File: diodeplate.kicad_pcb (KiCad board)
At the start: 2 copper layers, 86 parts, among them U1 TS-1185EC-C-D-B, U10 CP2102-GMR, U11 U262-16XN-4BVC11, U14 UMH3N, U2 TS-1185EC-C-D-B, U3 TS-1185EC-C-D-B, U8 ESP32-WROOM-32E(4MB), U9 SN74AHCT32QPWRQ1

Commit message: add first pcb design
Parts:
- removed C13: 10uF, Capacitor_SMD:C_0603_1608Metric_Pad1.08x0.95mm_HandSolder
- removed REF1: BL1117-33CX, footprint:SOT-223-4_L6.5-W3.5-P2.30-LS7.0-BR
- removed U10: CP2102-GMR, footprint:QFN-28_L5.0-W5.0-P0.50-BL-EP
- removed U11: U262-16XN-4BVC11, footprint:USB-3.1-SMD_U262-161N-4BVC11
- removed U14: UMH3N, footprint:SC-70-6_L2.2-W1.3-P0.65-LS2.1-BR
- removed U8: ESP32-WROOM-32E(4MB), footprint:WIFI-SMD_ESP32-WROOM-32E
- removed U9: SN74AHCT32QPWRQ1, footprint:TSSOP-14_L5.0-W4.4-P0.65-LS6.5-BL
- added SW1: TS-1185EC-C-D-B, footprint:SW-SMD_4P-L3.7-W3.0-P1.50-LS4.7, F.Cu at (170.8, 151.2)
- added SW2: TS-1185EC-C-D-B, footprint:SW-SMD_4P-L3.7-W3.0-P1.50-LS4.7, F.Cu at (171.0, 156.2)
- added SW3: TS-1185EC-C-D-B, footprint:SW-SMD_4P-L3.7-W3.0-P1.50-LS4.7, F.Cu at (170.8, 144.8)
- added U4: BL1117-33CX, footprint:SOT-223-4_L6.5-W3.5-P2.30-LS7.0-BR, F.Cu at (225.0, 186.5)
- added U5: UMH3N, footprint:SC-70-6_L2.2-W1.3-P0.65-LS2.1-BR, F.Cu at (223.7, 143.1)
- added U6: SN74AHCT32QPWRQ1, footprint:TSSOP-14_L5.0-W4.4-P0.65-LS6.5-BL, F.Cu at (188.5, 99.8)
- U1: value TS-1185EC-C-D-B -> ESP32-WROOM-32E; footprint footprint:SW-SMD_4P-L3.7-W3.0-P1.50-LS4.7 -> footprint:WIFI-SMD_ESP32-WROOM-32E
- U2: value TS-1185EC-C-D-B -> CP2102-GMR; footprint footprint:SW-SMD_4P-L3.7-W3.0-P1.50-LS4.7 -> footprint:QFN-28_L5.0-W5.0-P0.50-BL-EP
- U3: value TS-1185EC-C-D-B -> U262-161N-4BVC11; footprint footprint:SW-SMD_4P-L3.7-W3.0-P1.50-LS4.7 -> footprint:USB-3.1-SMD_U262-161N-4BVC11
- moved LED24 179.9 mm to (289.5, 126.9)
- moved LED20 173.1 mm to (280.3, 181.3)
- moved LED18 169.3 mm to (260.5, 202.8)
- moved LED25 163.6 mm to (285.4, 114.2)
- moved LED16 163.0 mm to (237.3, 214.1)
- moved LED19 157.8 mm to (272.3, 192.2)
- moved LED23 152.1 mm to (291.1, 142.6)
- moved LED21 149.9 mm to (285.5, 170.8)
- moved C16 149.8 mm to (232.2, 196.9), turned to 90 degrees
- moved LED17 146.0 mm to (248.9, 209.7)
- moved C30 145.1 mm to (287.1, 142.2), turned to -90 degrees
- moved C33 143.6 mm to (274.9, 101.4), turned to -90 degrees
- moved LED22 142.6 mm to (289.8, 156.6)
- moved LED29 142.0 mm to (252.6, 77.4)
- moved C29 139.1 mm to (285.9, 156.2), turned to -90 degrees
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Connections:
- C1 pad 1: GND -> +3V3
- C1 pad 2: +3V3 -> GND
- U1 pad 2: Net-(R4-Pad1) -> +3V3
- U2 pad 1: GND -> unconnected-(U2-Pad1)
- U2 pad 2: Net-(R5-Pad1) -> unconnected-(U2-Pad2)
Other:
- board outline added: 160 x 160 mm

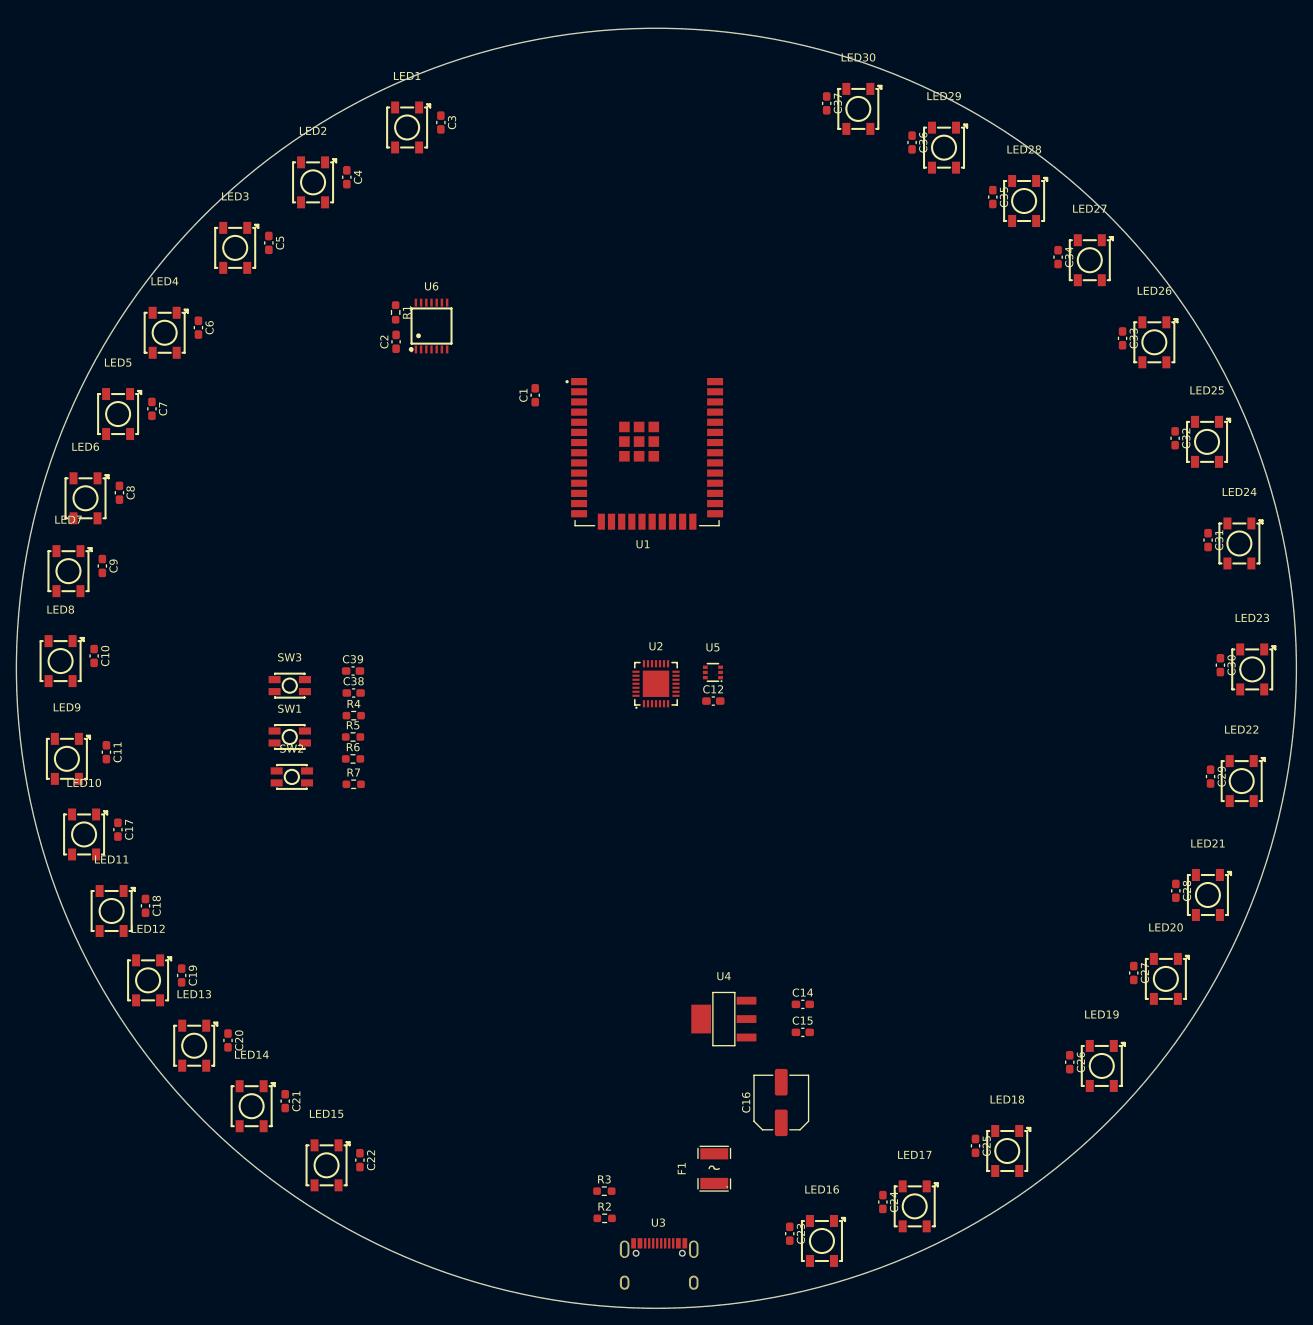
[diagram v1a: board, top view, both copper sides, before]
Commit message: leds arranged every 15cm
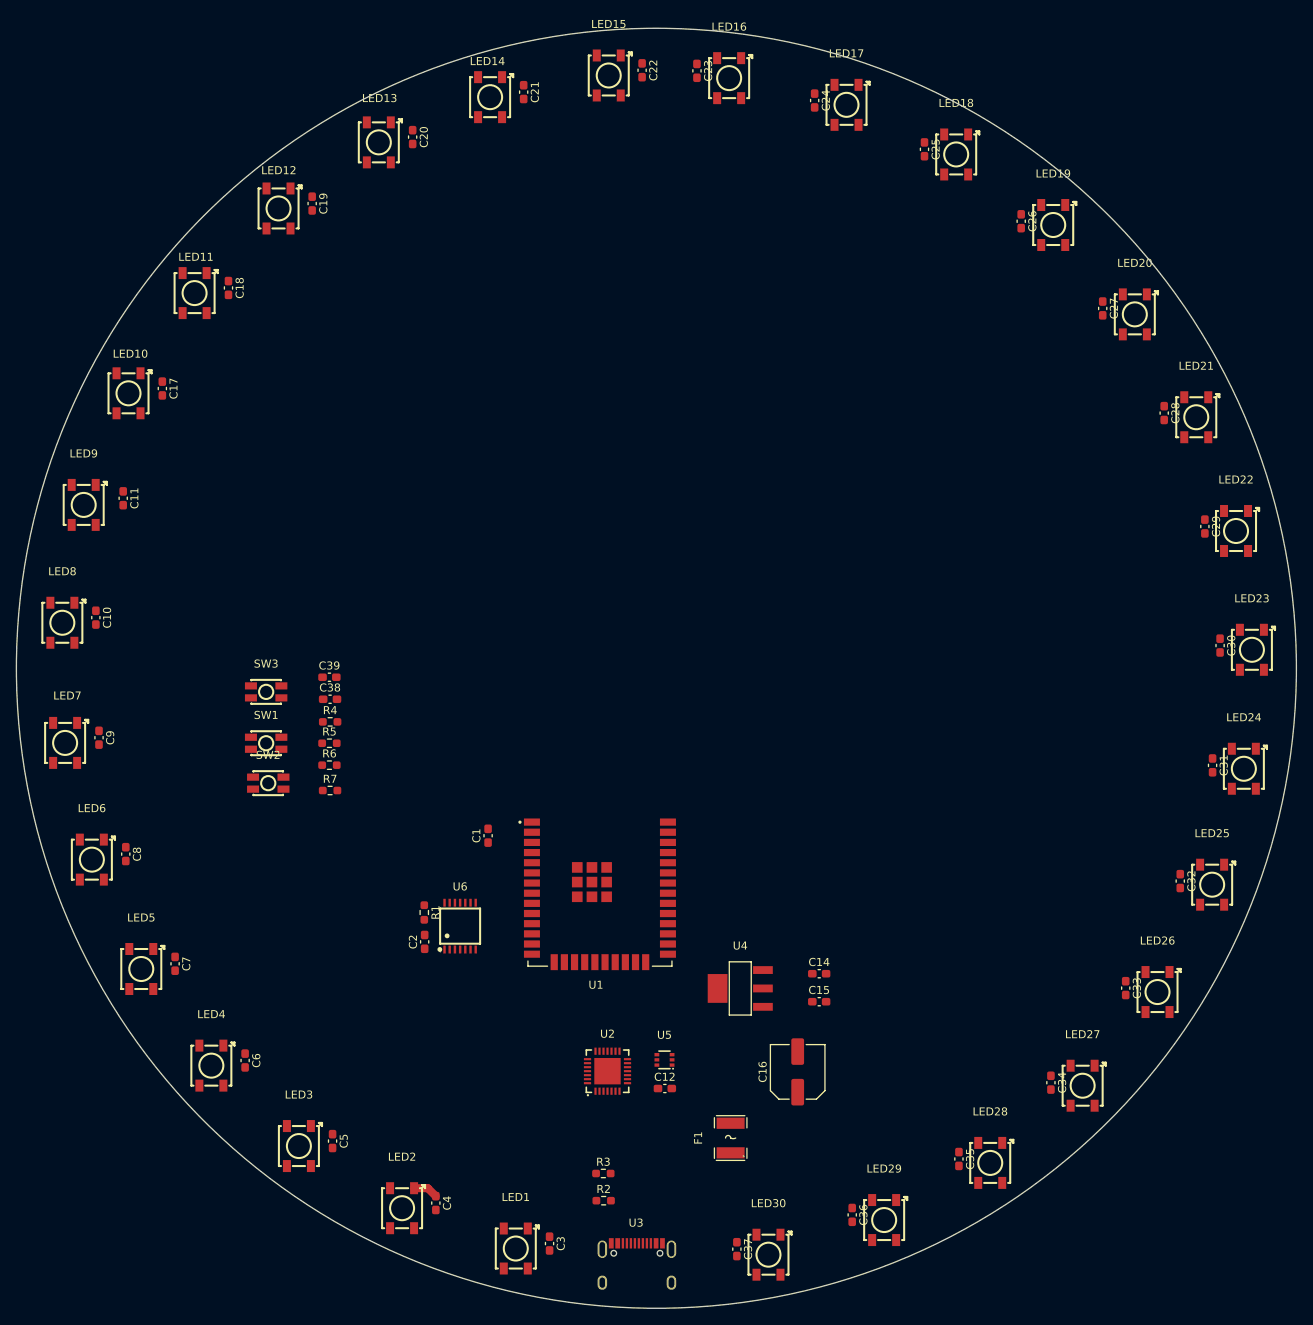
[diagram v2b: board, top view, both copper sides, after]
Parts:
- moved C23 145.8 mm to (221.7, 67.9)
- moved LED16 145.8 mm to (225.7, 68.7)
- moved LED30 143.7 mm to (230.6, 215.8)
- moved C37 143.7 mm to (226.7, 215.2)
- moved C3 140.8 mm to (203.2, 214.5)
- moved LED1 140.8 mm to (199.0, 215.0)
- moved C22 140.7 mm to (214.8, 67.9)
- moved LED15 140.7 mm to (210.6, 68.4)
- moved C24 138.0 mm to (236.4, 71.7)
- moved LED17 138.0 mm to (240.4, 72.0)
- moved C36 134.3 mm to (241.1, 210.9)
- moved LED29 134.3 mm to (245.1, 211.4)
- moved LED14 129.6 mm to (195.8, 71.1)
- moved C21 129.6 mm to (200.0, 70.6)
- moved C4 128.7 mm to (189.0, 209.5)
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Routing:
- net GND: track 0.00 -> 3.13 mm

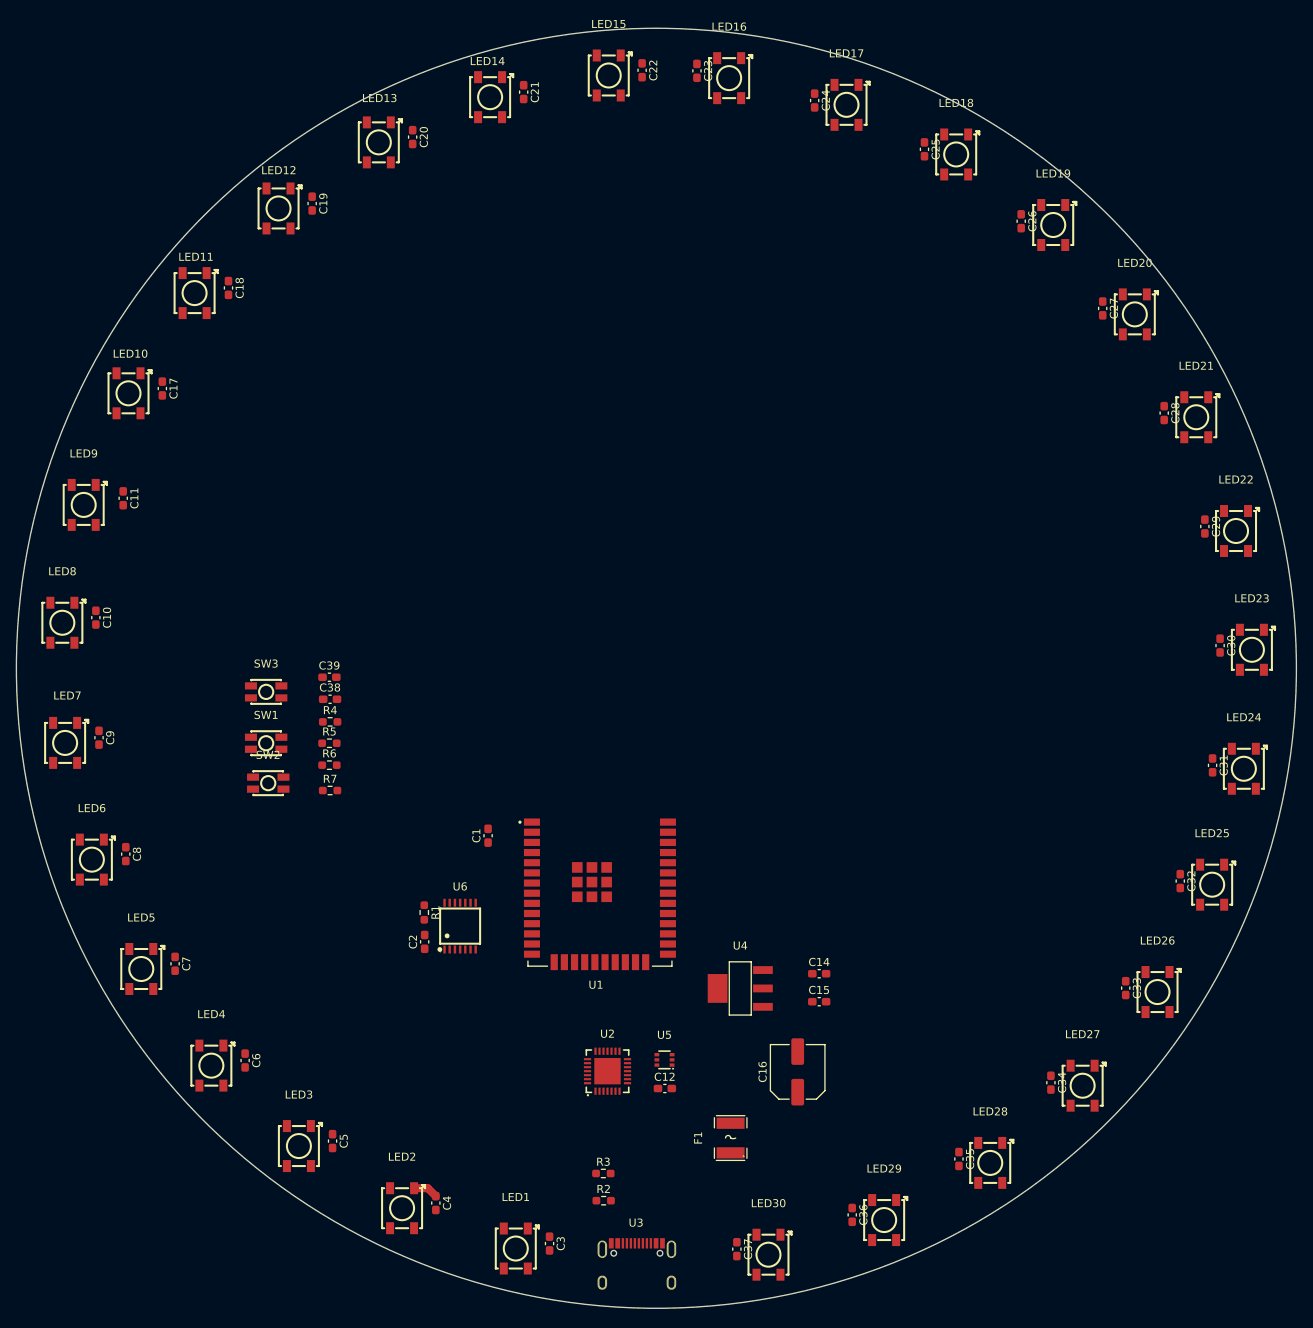
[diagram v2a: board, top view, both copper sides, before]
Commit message: finished traces, made plate bigger
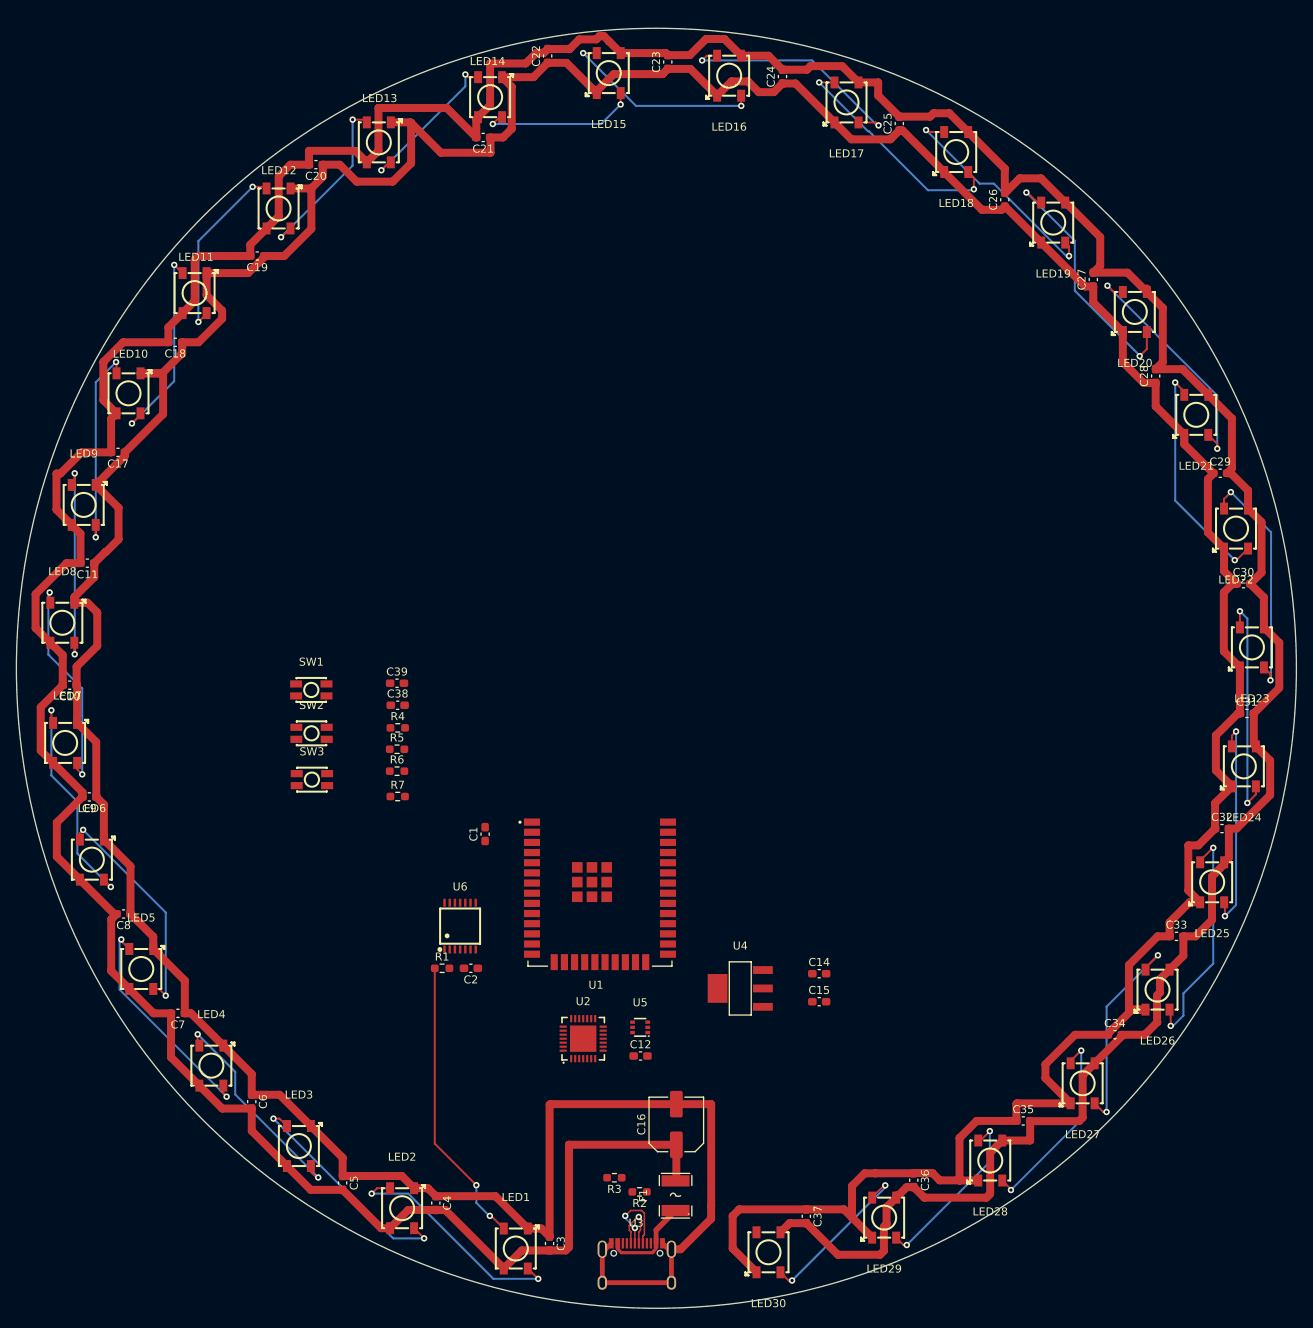
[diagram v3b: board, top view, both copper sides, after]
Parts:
- moved C16 16.5 mm to (219.1, 199.6)
- moved C20 12.6 mm to (174.0, 79.7), turned to 180 degrees
- moved SW3 12.4 mm to (173.5, 156.5)
- moved C22 11.9 mm to (203.0, 66.1), turned to 90 degrees
- moved C34 9.99 mm to (273.9, 188.4), turned to 0 degrees
- moved F1 9.97 mm to (219.0, 208.6)
- moved C17 9.72 mm to (149.3, 115.6), turned to 180 degrees
- moved C37 9.60 mm to (235.3, 211.1)
- moved C18 9.50 mm to (156.5, 101.9), turned to 180 degrees
- moved C19 9.50 mm to (166.7, 91.1), turned to 180 degrees
- moved C35 9.35 mm to (262.5, 199.2), turned to 0 degrees
- moved C11 9.27 mm to (145.5, 129.5), turned to 180 degrees
- moved C33 9.06 mm to (281.6, 176.1), turned to 0 degrees
- moved C10 9.05 mm to (143.3, 144.7), turned to 180 degrees
- moved C36 8.83 mm to (248.8, 206.6)
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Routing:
- net GND: track 3.13 -> 626.0 mm
- net +5V: track 0.00 -> 585.5 mm
- net LED DATA OUT: track 0.00 -> 36.4 mm, vias 0 -> 2
- net Net-(LED19-Pad2): track 0.00 -> 32.1 mm, vias 0 -> 2
- net Net-(LED20-Pad2): track 0.00 -> 30.5 mm, vias 0 -> 2
- net Net-(LED16-Pad2): track 0.00 -> 30.4 mm, vias 0 -> 2
- net Net-(LED22-Pad2): track 0.00 -> 30.0 mm, vias 0 -> 2
- net Net-(LED1-Pad2): track 0.00 -> 29.7 mm, vias 0 -> 2
- net Net-(LED21-Pad2): track 0.00 -> 29.6 mm, vias 0 -> 2
- net Net-(LED17-Pad2): track 0.00 -> 29.4 mm, vias 0 -> 2
- net Net-(LED25-Pad2): track 0.00 -> 29.2 mm, vias 0 -> 2
- net Net-(LED18-Pad2): track 0.00 -> 29.1 mm, vias 0 -> 2
- net Net-(LED23-Pad2): track 0.00 -> 28.9 mm, vias 0 -> 2
- net Net-(LED2-Pad2): track 0.00 -> 28.9 mm, vias 0 -> 2
- net Net-(LED4-Pad2): track 0.00 -> 28.4 mm, vias 0 -> 2
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
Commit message: add jlcpscb folder
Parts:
- moved C39 59.2 mm to (219.1, 192.3), turned to -90 degrees
- moved SW2 35.7 mm to (186.3, 184.1)
- moved C38 33.1 mm to (202.6, 174.8), turned to -90 degrees
- moved R5 32.8 mm to (191.2, 184.8)
- moved SW1 29.7 mm to (186.2, 172.2)
- moved U2 27.6 mm to (234.4, 183.1)
- moved R7 25.9 mm to (193.1, 183.1)
- moved SW3 25.1 mm to (186.3, 178.2)
- moved R4 23.8 mm to (191.2, 172.8)
- moved U6 23.0 mm to (192.6, 197.9), turned to 90 degrees
- moved C14 21.5 mm to (228.4, 200.6), turned to 90 degrees
- moved R1 21.4 mm to (199.1, 199.5), turned to 90 degrees
- moved U4 20.9 mm to (234.9, 202.0), turned to 180 degrees
- moved C12 20.5 mm to (235.1, 190.7)
- moved C2 19.8 mm to (187.5, 199.0), turned to -90 degrees
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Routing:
- net GND: track 626.0 -> 844.1 mm, vias 0 -> 3
- net +3V3: track 0.00 -> 102.9 mm, vias 0 -> 3
- net +5V: track 585.5 -> 665.0 mm, vias 0 -> 6
- net RESET: track 0.00 -> 47.9 mm, vias 0 -> 2
- net IO0: track 0.00 -> 42.8 mm
- net IO16/LED1: track 0.00 -> 39.1 mm, vias 0 -> 2
- net USB-C DATA +: track 10.6 -> 49.2 mm, vias 2 -> 3
- net USB-C DATA -: track 7.41 -> 45.6 mm, vias 1 -> 2
- net LED DATA OUT: track 36.4 -> 13.7 mm
- net IO33/MAINBUTTON: track 0.00 -> 21.7 mm
- net TXD: track 0.00 -> 16.7 mm
- net RXD: track 0.00 -> 15.5 mm
- net USB-C CC1: track 0.00 -> 10.6 mm
- net VBUS: track 11.7 -> 21.5 mm, vias 0 -> 2
- net USB-C CC2: track 0.03 -> 8.53 mm
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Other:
- board size 160 x 160 mm -> 164 x 164 mm

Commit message: added groundplate, update gitignore
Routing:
- added copper zone on B.Cu, net GND
- added copper zone on F.Cu, net GND
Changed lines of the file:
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@@
   (segment (start 213.91 212.58) (end 212.71 211.38) (width 0.2) (layer "B.Cu") (net 50))
   (segment (start 212.71 211.07) (end 212.71 208.55) (width 0.2) (layer "B.Cu") (net 50))
+  (zone (net 1) (net_name "GND") (layers F&B.Cu) (hatch edge 0.508)
+    (connect_pads (clearance 0.508))
+    (min_thickness 0.254) (filled_areas_thickness no)
+    (fill yes (thermal_gap 0.508) (thermal_bridge_width 0.508))
+    (polygon
+      (pts
+        (xy 579.69 409.69)
+        (xy 12.84 409.69)
+        (xy 12.84 12.03)
+        (xy 579.69 12.03)
+      )
+    )
+  )
+  (zone (net 0) (net_name "") (layers F&B.Cu) (hatch edge 0.508)
+    (connect_pads (clearance 0))
+    (min_thickness 0.254)
+    (keepout (tracks not_allowed) (vias not_allowed) (pads not_allowed ) (copperpour not_allowed) (footprints allowed))
+    (fill (thermal_gap 0.508) (thermal_bridge_width 0.508))
+    (polygon
+      (pts
+        (xy 238.86 168.45)
+        (xy 188.6 168.45)
+        (xy 188.6 149.68)
+        (xy 238.86 149.68)
+      )
+    )
+  )
 )
